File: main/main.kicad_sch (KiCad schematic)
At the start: 83 parts, among them J1 3.5mm Jack, J2 3.5mm Jack, J3 3.5mm Jack, J4 3.5mm Jack, J5 3.5mm Jack, J6 2x5 Header, J7 3.5mm Jack, Q1 MMBT3904, Q2 MMBT3904, Q3 MMBT3904, U1 TL072CP, U2 AMS1117-5.0, U3 TL072CP, U4 LM317_SOT-223, U5 TL072CP

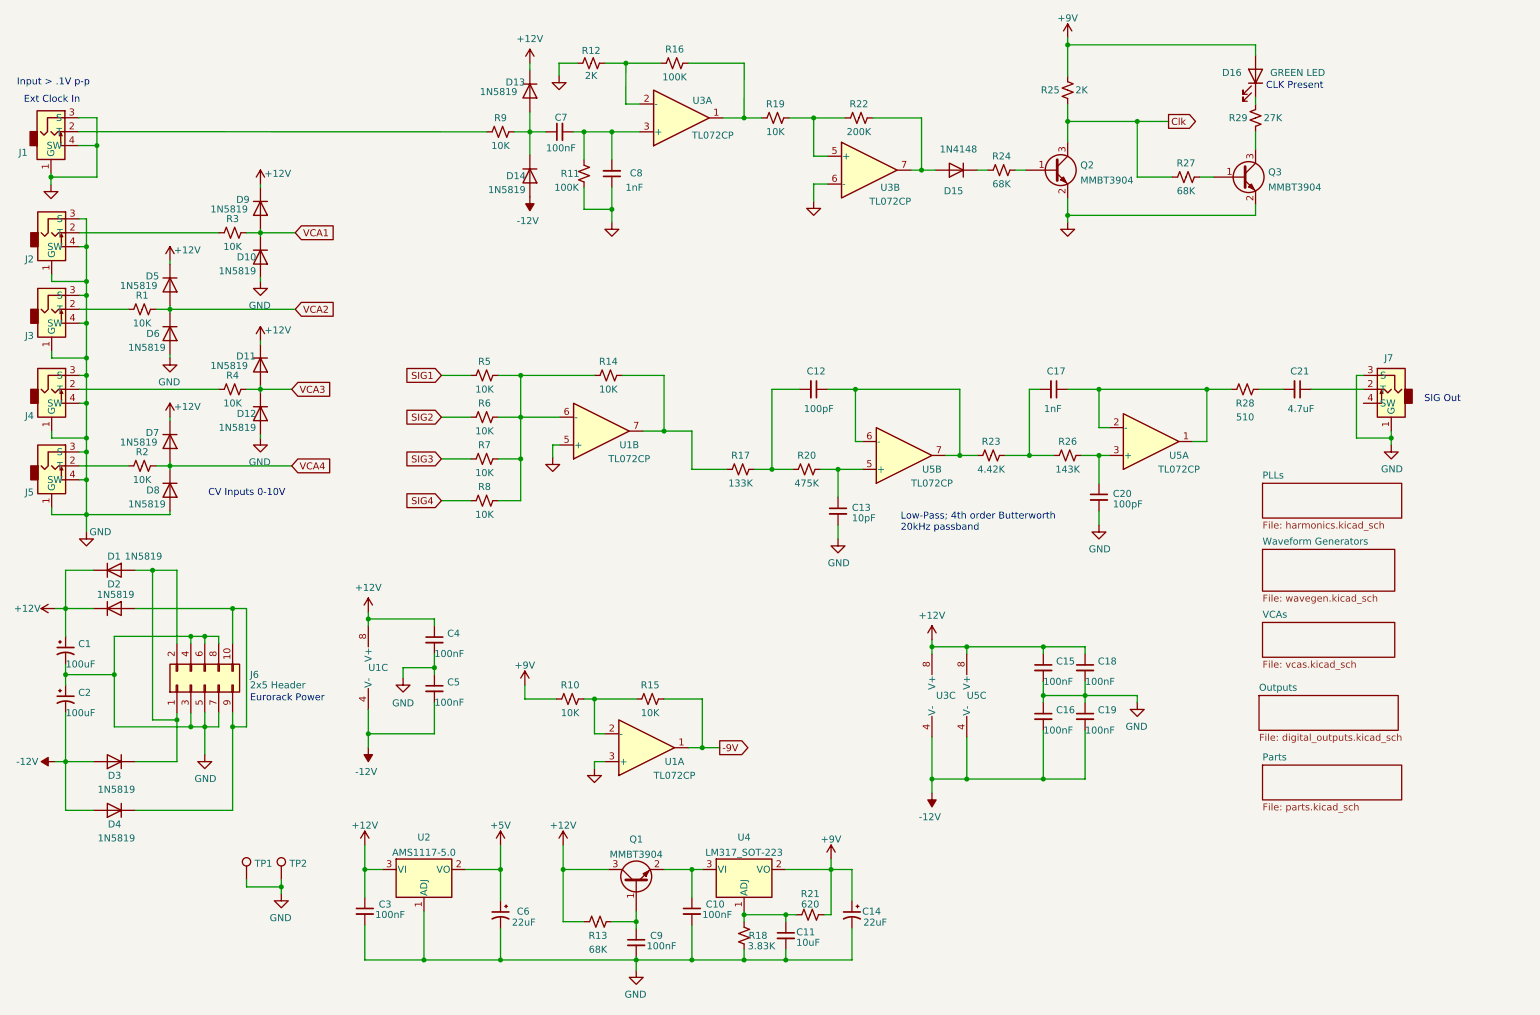
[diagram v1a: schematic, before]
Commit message: Switch to Thonk jacks.
Reduces use of extended parts.
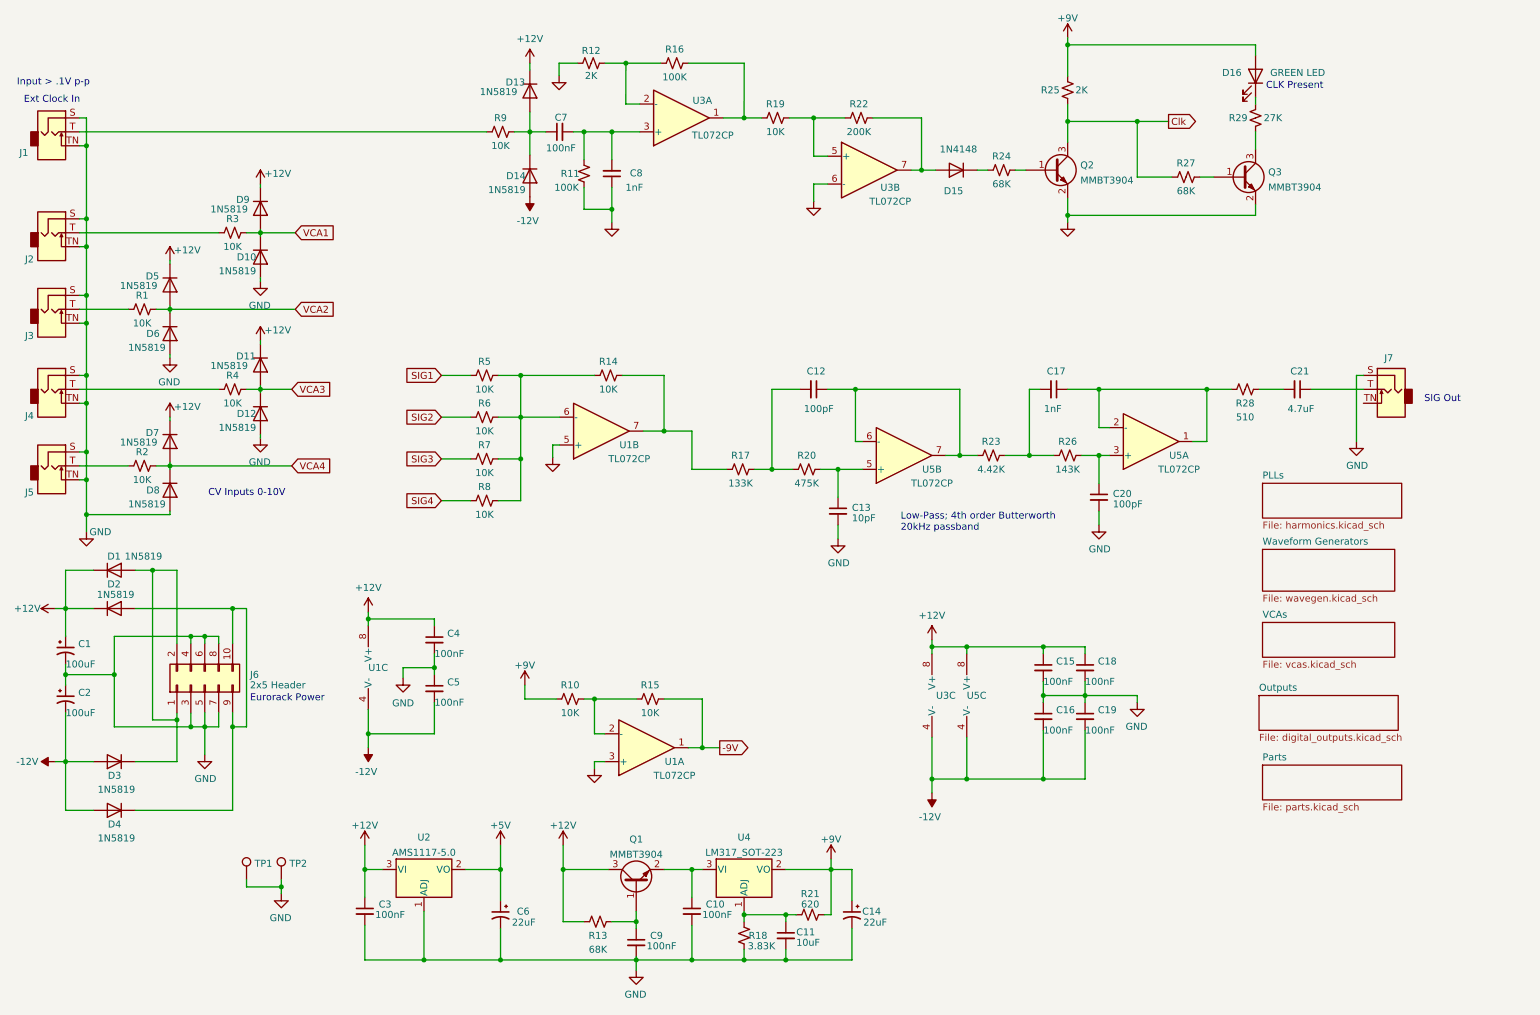
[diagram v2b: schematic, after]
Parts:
- C13: footprint Capacitor_SMD:C_0805_2012Metric_Pad1.18x1.45mm_HandSolder -> Capacitor_SMD:C_0603_1608Metric_Pad1.08x0.95mm_HandSolder; LCSC Part # C107107 -> C1634
- C17: LCSC Part # C597357 -> C46653
- D10, D11, D12, D13, D14, D5, D6, D7, D8, D9: footprint Diode_SMD:D_0805_2012Metric_Pad1.15x1.40mm_HandSolder -> Diode_SMD:D_SOD-323_HandSoldering
- D15: LCSC Part # C2892570 -> C81598
- J1, J2, J3, J4, J5, J7: footprint sputterizer:Molex-0472570001 -> audio jacks:Jack_3.5mm_QingPu_WQP-PJ398SM_Vertical; symbol greenface-symbols:Molex_47257 -> Connector:AudioJack2_SwitchT
- U1, U3, U5: LCSC Part # C67473 -> C6961
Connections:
- net GND: now also J1.S, J1.TN, J2.S, J2.TN, J3.S, J3.TN, J4.S, J4.TN, J5.S, J5.TN, J7.S; no longer J1.1 (G), J1.3 (S), J1.4 (SW), J2.1 (G), J2.3 (S), J2.4 (SW), J3.1 (G), J3.3 (S), J3.4 (SW), J4.1 (G), J4.3 (S), J4.4 (SW), J5.1 (G), J5.3 (S), J5.4 (SW), J7.1 (G), J7.3 (S)
- net at R3.2: now also J2.T; no longer J2.2 (T)
- net at R9.2: now also J1.T; no longer J1.2 (T)
- net at R2.2: now also J5.T; no longer J5.2 (T)
- net at C21.1: now also J7.T; no longer J7.2 (T)
- net at R1.2: now also J3.T; no longer J3.2 (T)
- net at R4.2: now also J4.T; no longer J4.2 (T)

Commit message: Version 1.0
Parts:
- removed C21: 4.7uF, Capacitor_SMD:C_1206_3216Metric, symbol Device:C_Small
- removed C9: 100nF, Capacitor_SMD:C_0805_2012Metric_Pad1.18x1.45mm_HandSolder, symbol Device:C_Small
- removed Q1, Q3: MMBT3904, Package_TO_SOT_SMD:SOT-23, symbol Transistor_BJT:MMBT3904
- added D29, D30: 1N5819, Diode_SMD:D_SOD-323_HandSoldering, symbol Diode:1N4148
- added Q3: MMBT3906, Package_TO_SOT_SMD:SOT-23, symbol Transistor_BJT:MMBT3906
- added R190: 100K, Resistor_SMD:R_0603_1608Metric, symbol Device:R_Small_US
- added TP3: TestPoint, TestPoint:TestPoint_Loop_D2.54mm_Drill1.5mm_Beaded, symbol Connector:TestPoint
- C17: LCSC Part # C46653 -> C62774
- C8: value 1nF -> 3.9nF; LCSC Part # C46653 -> C541576
- R10, R15: value 10K -> 100K; LCSC Part # C25804 -> C25803
- R13: value 68K -> 91K; footprint Resistor_SMD:R_0805_2012Metric_Pad1.20x1.40mm_HandSolder -> Resistor_SMD:R_0603_1608Metric; Digi-Key Part CF14JT68K0CT-ND -> CRT0805-FZ-1002ELFCT-ND; LCSC Part # C17801 -> C23265
- R23: value 4.42K -> 4.7K; LCSC Part # C23043 -> C23162
- R29: value 27K -> 1K; footprint Resistor_SMD:R_0805_2012Metric_Pad1.20x1.40mm_HandSolder -> Resistor_SMD:R_0603_1608Metric; LCSC Part # C17593 -> C21190
- TP1, TP2: footprint TestPoint:TestPoint_Keystone_5005-5009_Compact -> TestPoint:TestPoint_Loop_D2.54mm_Drill1.5mm_Beaded
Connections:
- net +12V: now also C10.1, U4.3 (VI), D29.1 (K); no longer R13.2
- net +9V: now also R13.2, Q3.2 (E); no longer D16.2 (A)
- net -12V: now also D30.2 (A)
- net -9V: now also R190.1
- net Clk: now also TP3.1
- net GND: now also R29.1; no longer U3.6 (-)
- net at C17.1, R28.1, U5.1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: now also D29.2 (A), D30.1 (K)
- net at R28.2: now also J7.T
- net at R13.1: now also U3.6 (-), R190.2
- net at R27.1: now also Q3.1 (B)
- new net: D16.2 (A), Q3.3 (C)
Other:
- added sheet Filters (filters.kicad_sch)
- added sheet Hi Pass Filters (hipass.kicad_sch)
- note added: "-3dB @ 30KHz"
- title: Pipes (main) -> Twangilizer
- moved on the sheet: C1, C10, C15, C16, C18, C19, C2, C4, C5, D1, D16, D2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

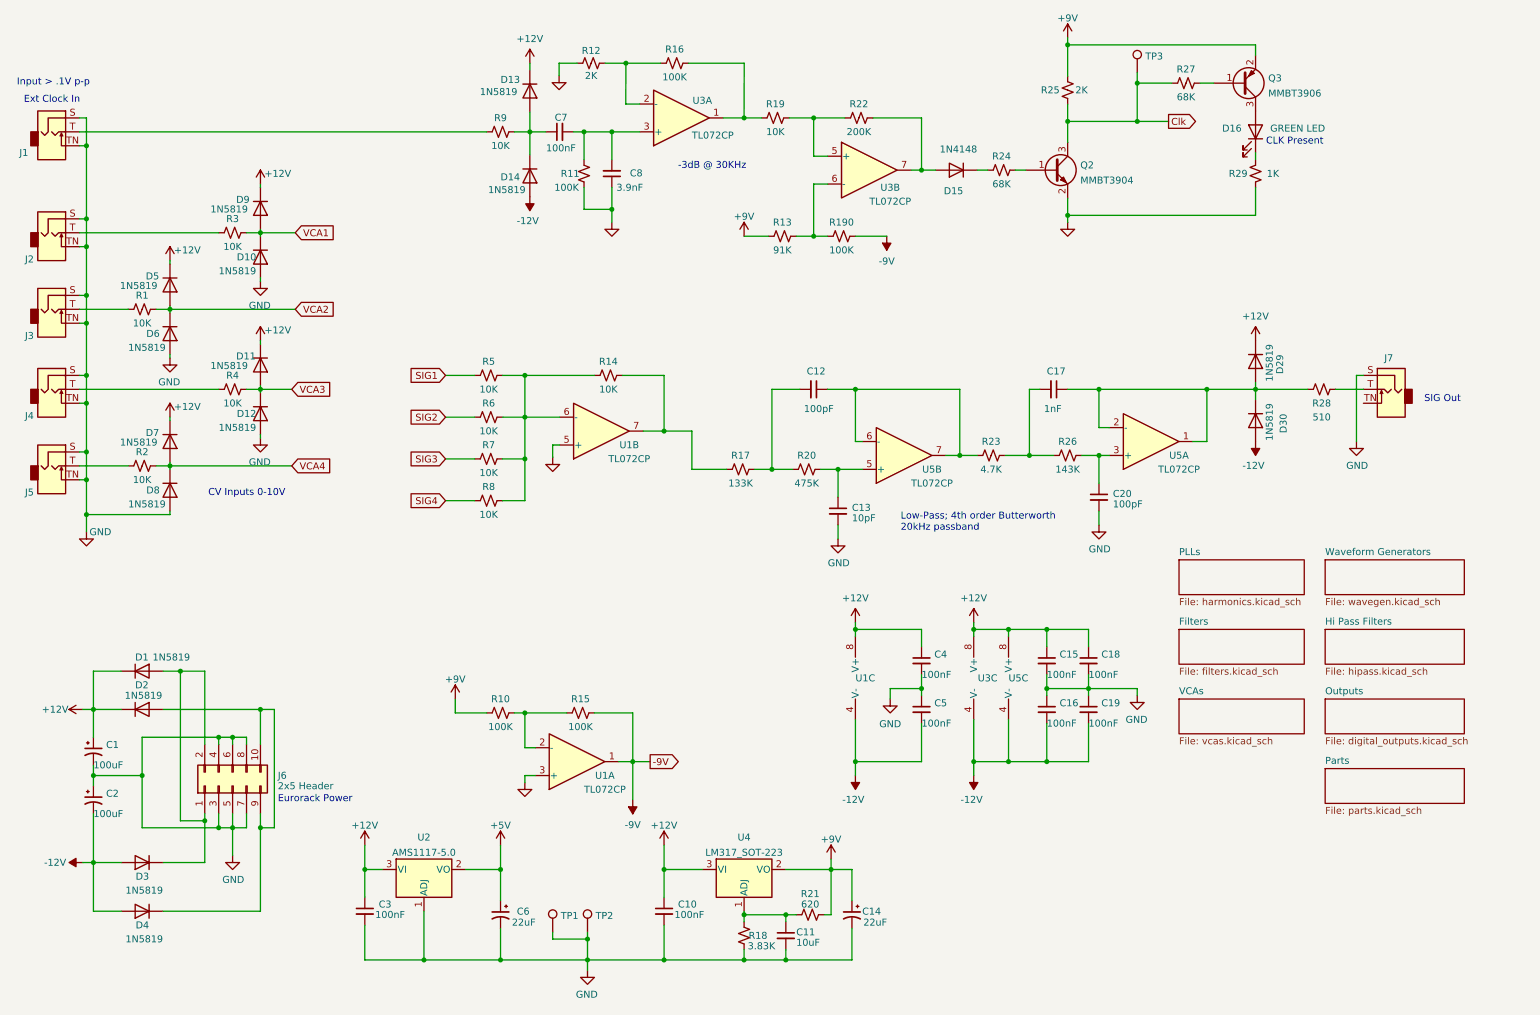
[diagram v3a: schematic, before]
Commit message: v1.0
Docs still need work.
Oscillators.sch not used. Saved just in case.
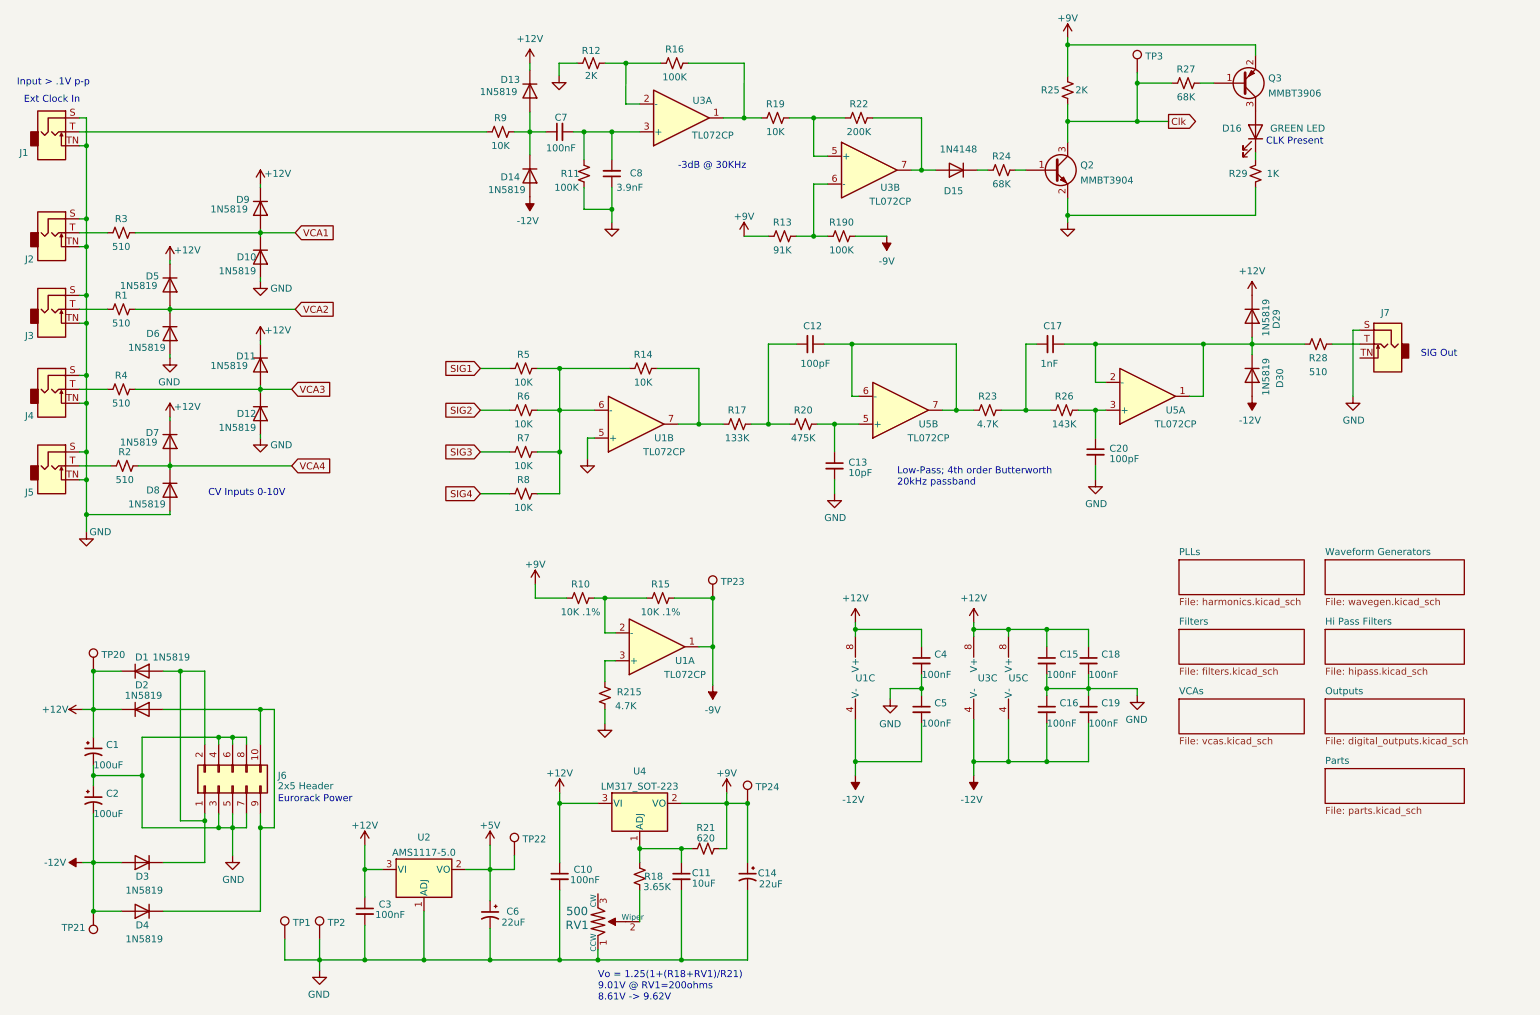
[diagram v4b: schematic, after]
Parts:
- added R215: 4.7K, Resistor_SMD:R_0603_1608Metric, symbol Device:R_Small_US
- added RV1: 500, sputterizer:HDK_3mm, symbol dk_Trimmer-Potentiometers:TC33X-2-103E
- added TP20, TP21, TP22, TP23, TP24: TestPoint, TestPoint:TestPoint_Loop_D2.54mm_Drill1.5mm_Beaded, symbol Connector:TestPoint
- R1, R2, R3, R4: value 10K -> 510; footprint Resistor_SMD:R_0603_1608Metric -> Resistor_SMD:R_0805_2012Metric_Pad1.20x1.40mm_HandSolder; LCSC Part # C25804 -> C2842425
- R10, R15: value 100K -> 10K .1%; LCSC Part # C25803 -> C95204
- R18: value 3.83K -> 3.65K; footprint Resistor_SMD:R_0805_2012Metric_Pad1.20x1.40mm_HandSolder -> Resistor_SMD:R_0603_1608Metric_Pad0.98x0.95mm_HandSolder; LCSC Part # C483108 -> C137730
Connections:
- net +12V: now also TP20.1
- net +5V: now also TP22.1
- net +9V: now also TP24.1
- net -12V: now also TP21.1
- net -9V: now also TP23.1
- net GND: now also R215.2, RV1.1 (CCW); no longer R18.2, U1.3 (+)
- new net: R215.1, U1.3 (+)
- new net: R18.2, RV1.2 (Wiper)
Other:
- note added: "Vo = 1.25(1+(R18+RV1)/R21) 9.01V @ RV1=200ohms 8.61V -> 9.62V"
- moved on the sheet: C10, C11, C12, C13, C14, C17, C20, C6, D29, D30, J7, R1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

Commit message: Work in progress
Adds User Manual
Changes CV range to 0 - 8V
Adds spice vactrol test circuit.
Adds VCA spice study
Updates other spice and excel files.
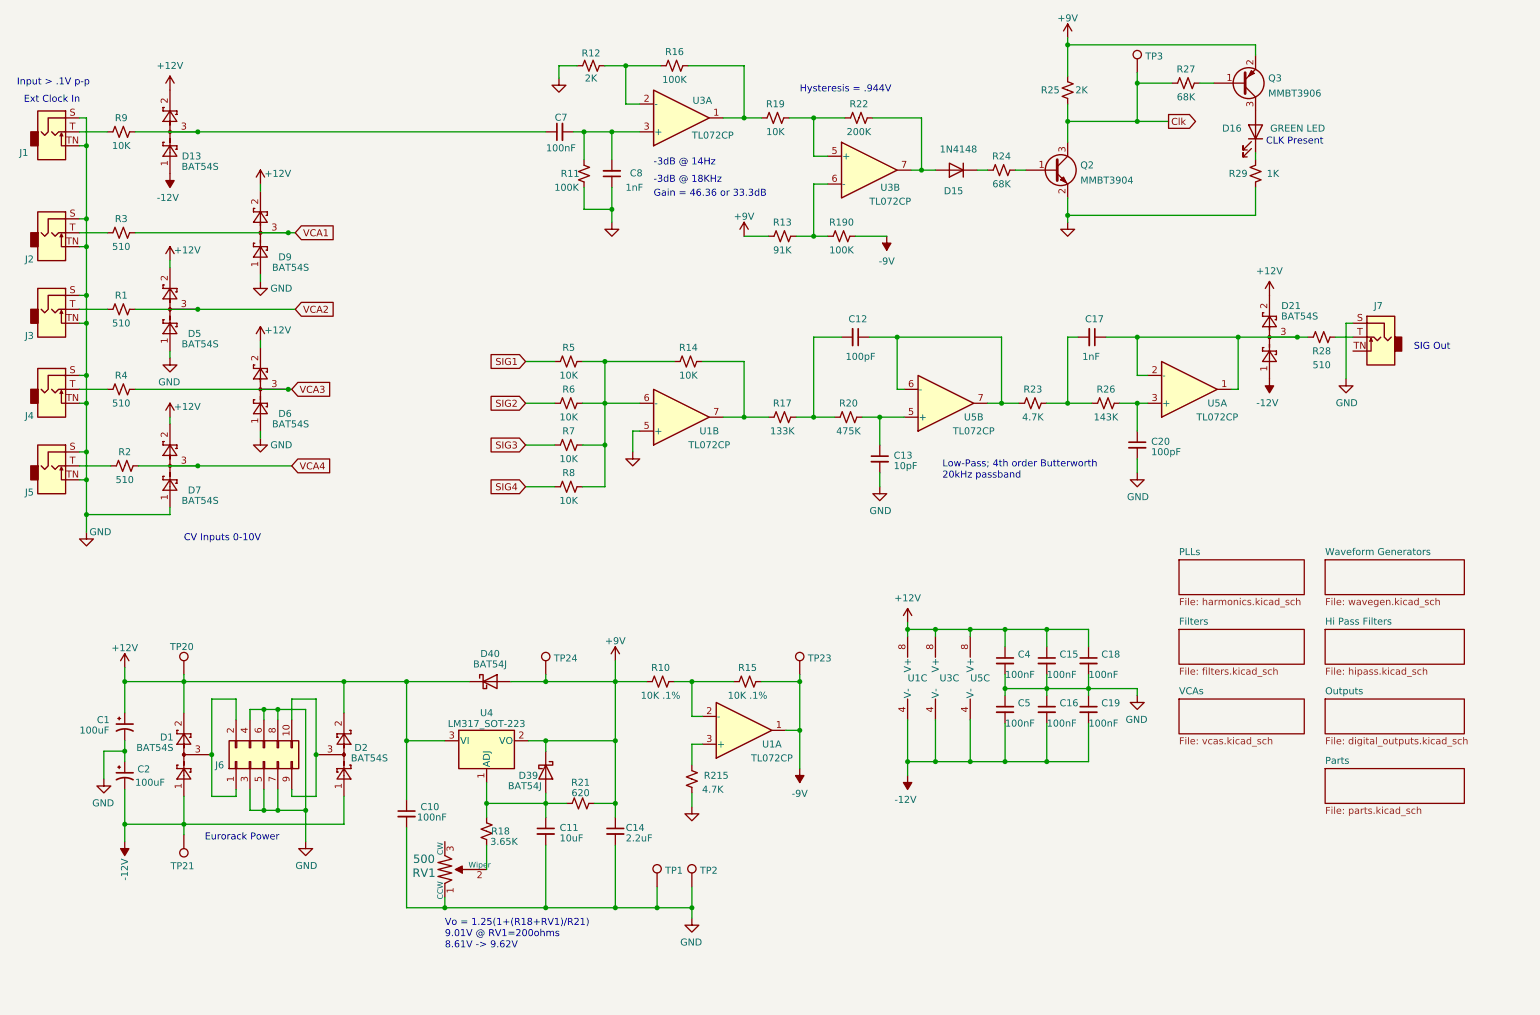
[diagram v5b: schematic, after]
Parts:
- removed C14, C6: 22uF, Capacitor_Tantalum_SMD:CP_EIA-3216-18_Kemet-A, symbol Device:CP1_Small
- removed C3: 100nF, Capacitor_SMD:C_0805_2012Metric_Pad1.18x1.45mm_HandSolder, symbol Device:C_Small
- removed D1, D10, D11, D12, D13, D14, D2, D29, D3, D30, D4, D5, D6, D7, D8, D9: 1N5819, Diode_SMD:D_SOD-323_HandSoldering, symbol Diode:1N4148
- removed TP22: TestPoint, TestPoint:TestPoint_Loop_D2.54mm_Drill1.5mm_Beaded, symbol Connector:TestPoint
- removed U2: AMS1117-5.0, Package_TO_SOT_SMD:SOT-223-3_TabPin2, symbol Regulator_Linear:LM317_SOT-223
- added C14: 2.2uF, Capacitor_SMD:C_0603_1608Metric_Pad1.08x0.95mm_HandSolder, symbol Device:C_Small
- added D1, D13, D2, D21, D5, D6, D7, D9: BAT54S, Package_TO_SOT_SMD:SOT-23, symbol Diode:BAT54S
- added D39, D40: BAT54J, Diode_SMD:D_SOD-323F, symbol Diode:BAT54J
- C8: value 3.9nF -> 1nF; LCSC Part # C541576 -> C62774
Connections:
- net +12V: now also D1.2, D13.2, D2.2, D21.2, D40.1 (K), D5.2, D6.2, D7.2, D9.2
- net +9V: now also C14.1, D39.1 (K), D40.2 (A)
- net -12V: now also D1.1, D13.1, D2.1, D21.1
- net GND: now also C14.2, D5.1, D6.1, D7.1, D9.1
- net VCA1: now also D9.3
- net VCA2: now also D5.3
- net VCA3: now also D6.3
- net VCA4: now also D7.3
- net at C17.1, R28.1, U5.1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: now also D21.3
- net at C11.1, R18.1, R21.2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: now also D39.2 (A)
- net at C7.1, R9.1: now also D13.3
- net at J6.10 (Pin_10), J6.9 (Pin_9): now also D2.3
- net at J6.1 (Pin_1), J6.2 (Pin_2): now also D1.3
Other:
- note added: "-3dB @ 14Hz"
- note added: "-3dB @ 18KHz"
- note added: "Gain = 46.36 or 33.3dB"
- note added: "Hysteresis = .944V"
- note removed: "-3dB @ 30KHz"
- moved on the sheet: C1, C10, C11, C12, C13, C17, C2, C20, C4, C5, J6, J7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
